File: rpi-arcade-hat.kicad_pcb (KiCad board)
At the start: 2 copper layers, 41.9 x 73.7 mm, 12 parts, among them J1 RASPBERRYPI-40-PIN-GPIO_ARCADE, J2 P2_Joystick, J3 P2_Buttons_ABXY, J4 P2_Buttons_SLSTLR, J5 P1_Joystick, J6 P1_Buttons_ABXY, J7 P1_Buttons_SLSTLR, J8 Hotkey_GNDs

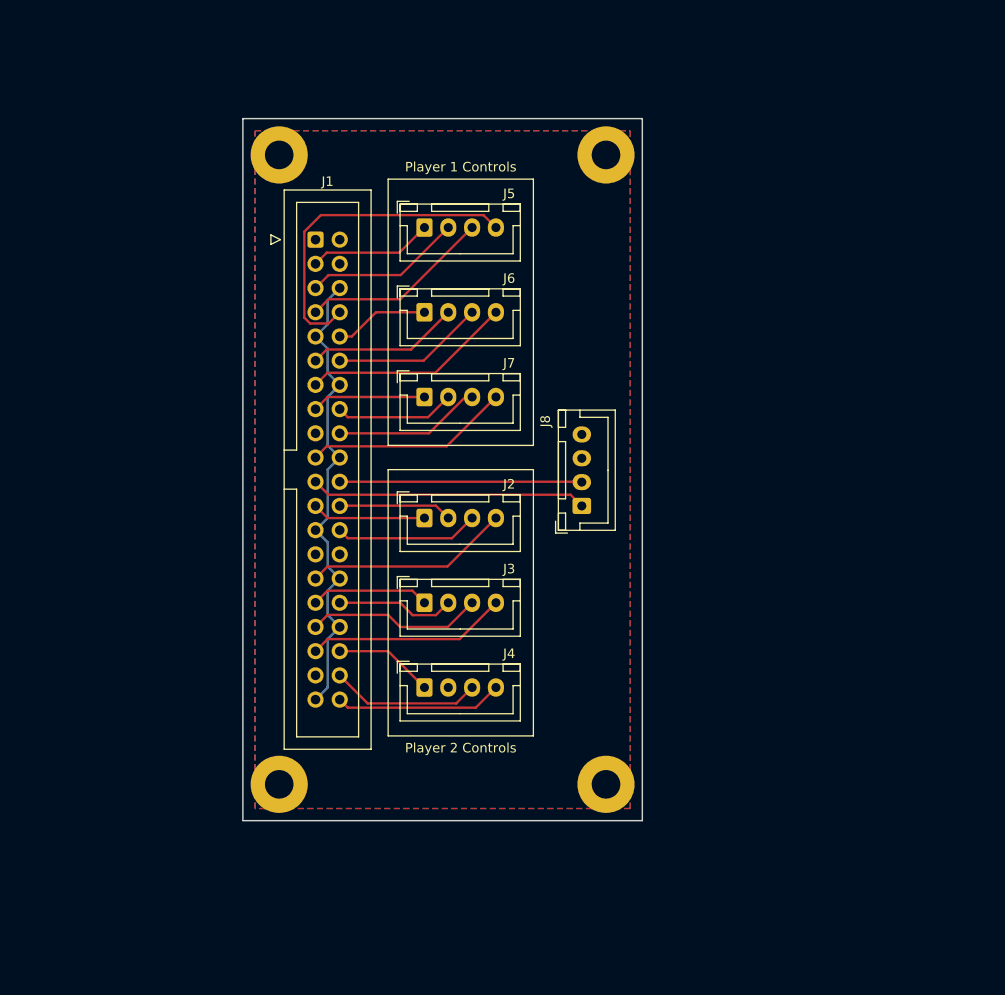
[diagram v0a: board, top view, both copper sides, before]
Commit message: Added 100mm PCBWay layout
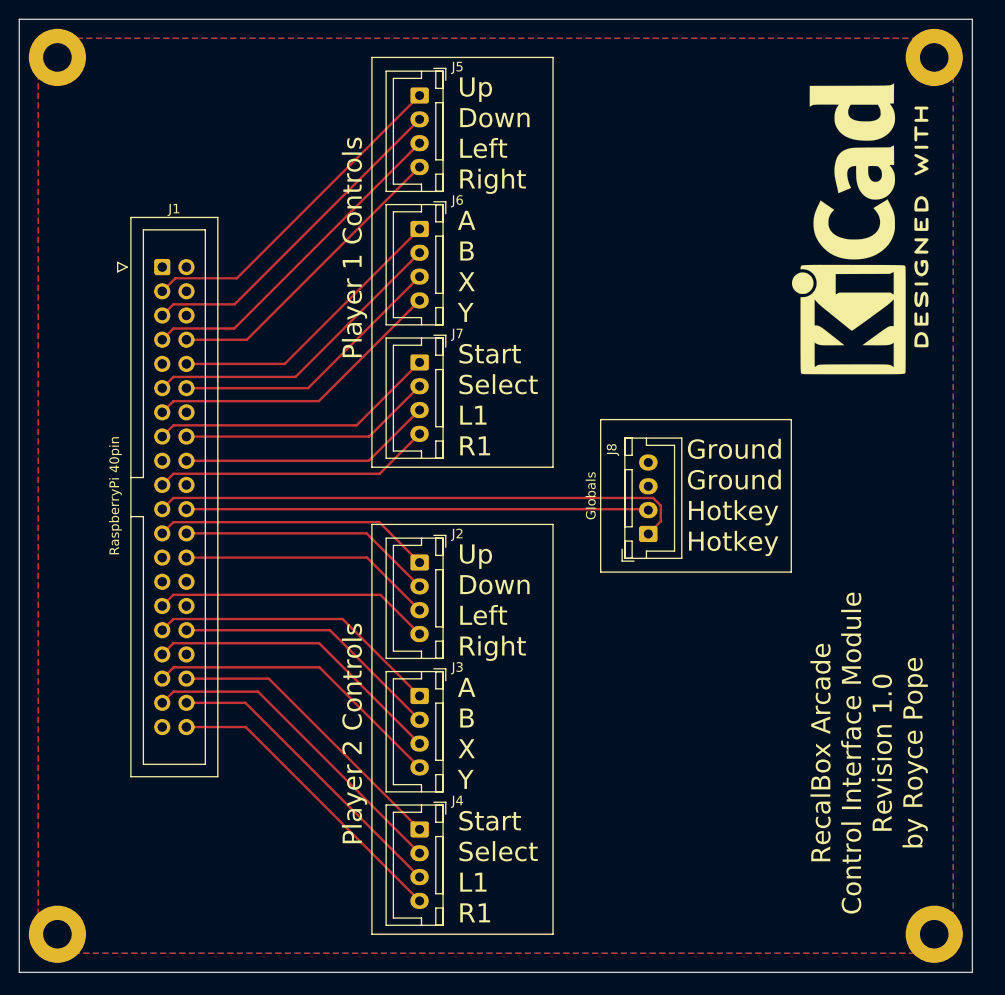
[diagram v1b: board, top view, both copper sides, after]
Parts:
- added REF**: KiCad-Logo2_12mm_SilkScreen, Symbol:KiCad-Logo2_12mm_SilkScreen, F.Cu at (188.0, 70.0)
- moved REF** 37.9 mm to (197.0, 144.0)
- moved REF** 35.9 mm to (197.0, 52.0)
- moved REF** 28.1 mm to (105.0, 144.0)
- moved REF** 25.4 mm to (105.0, 52.0)
- moved J1 16.3 mm to (116.0, 74.0)
- moved J4 14.9 mm to (143.0, 133.0), turned to 270 degrees
- moved J5 13.9 mm to (143.0, 56.0), turned to 270 degrees
- moved J3 9.79 mm to (143.0, 119.0), turned to 270 degrees
- moved J6 8.75 mm to (143.0, 70.0), turned to 270 degrees
- moved J8 7.57 mm to (167.0, 102.0)
- moved J2 4.70 mm to (143.0, 105.0), turned to 270 degrees
- moved J7 3.67 mm to (143.0, 84.0), turned to 270 degrees
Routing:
- net GND: track 50.5 -> 0.00 mm
- net Net-(J1-Pad37): track 0.00 -> 34.5 mm
- net Net-(J1-Pad21): track 29.0 -> 56.6 mm
- net Net-(J1-Pad22): track 25.4 -> 48.5 mm
- net Net-(J1-Pad3): track 13.0 -> 35.5 mm
- net Net-(J1-Pad36): track 10.5 -> 31.0 mm
- net Net-(J1-Pad10): track 9.94 -> 30.3 mm
- net Net-(J1-Pad5): track 16.6 -> 35.5 mm
- net Net-(J1-Pad31): track 12.5 -> 30.8 mm
- net Net-(J1-Pad15): track 12.0 -> 30.2 mm
- net Net-(J1-Pad23): track 12.0 -> 29.2 mm
- net Net-(J1-Pad11): track 16.0 -> 32.9 mm
- net Net-(J1-Pad38): track 15.8 -> 32.0 mm
- net Net-(J1-Pad32): track 12.5 -> 28.4 mm
- net Net-(J1-Pad7): track 20.1 -> 35.5 mm
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- added copper zone on F.Cu, net (none)
- removed copper zone on F.Cu, net Net-(J1-Pad10)
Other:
- board size 41.9 x 73.7 mm -> 100 x 100 mm
- board text added: "A B X Y"
- board text added: "Globals"
- board text added: "Ground Ground Hotkey Hotkey"
- board text added: "RaspberryPi 40pin"
- board text added: "RecalBox Arcade Control Interface Module Revision 1.0 by Royce Pope"
- board text added: "Start Select L1 R1"
- board text added: "Up Down Left Right"

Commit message: Add Part numbers, modify silkscreen, remove unused layers.
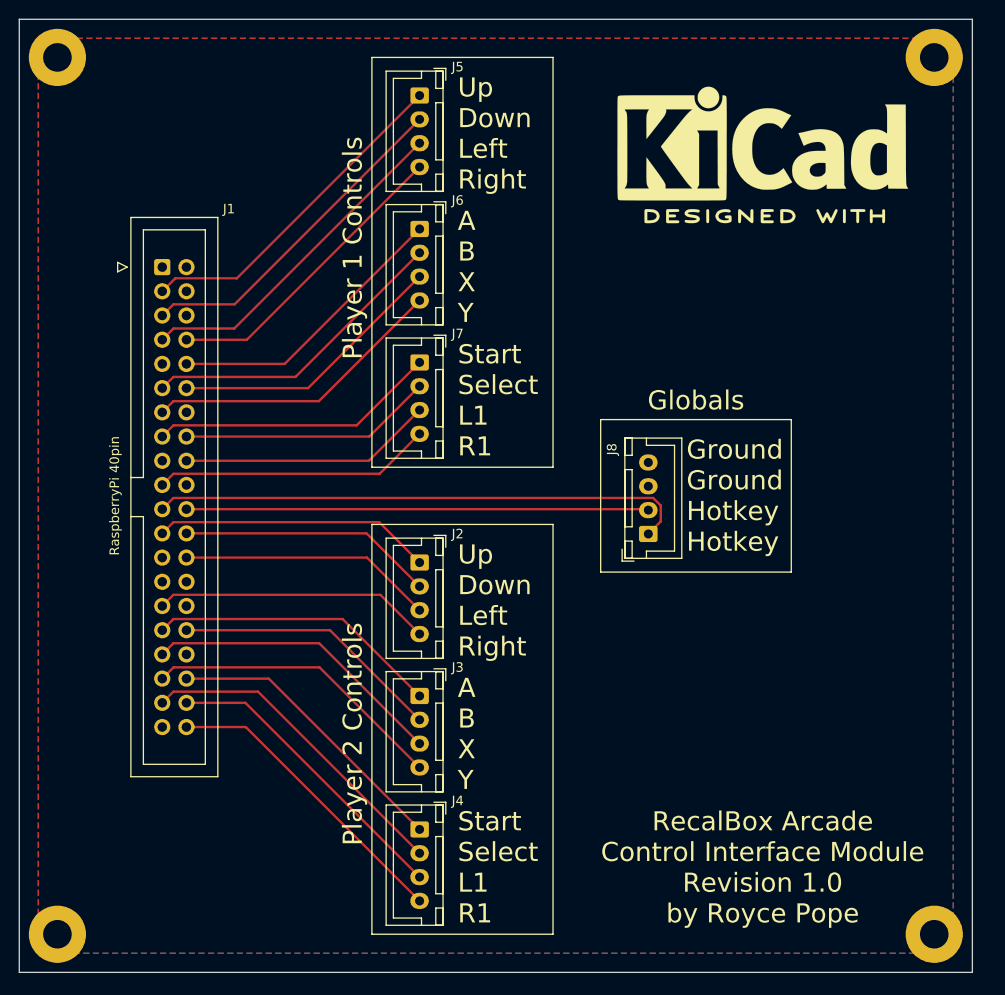
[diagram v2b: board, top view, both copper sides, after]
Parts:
- moved REF** 12.7 mm to (179.0, 61.0), turned to 0 degrees
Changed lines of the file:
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@@
     (0 F.Cu signal)
     (31 B.Cu power)
-    (33 F.Adhes user)
-    (35 F.Paste user)
     (37 F.SilkS user)
     (38 B.Mask user)
     (39 F.Mask user)
-    (40 Dwgs.User user)
     (41 Cmts.User user)
-    (42 Eco1.User user)
-    (43 Eco2.User user)
     (44 Edge.Cuts user)
     (45 Margin user)
-    (46 B.CrtYd user)
+    (46 B.CrtYd user hide)
     (47 F.CrtYd user)
     (49 F.Fab user hide)
@@
   )
   (module Symbol:KiCad-Logo2_12mm_SilkScreen (layer F.Cu)
-    (at 188 70 90)
+    (at 179 61)
     (descr "KiCad Logo")
     (tags "Logo KiCad")
     (attr virtual)
-    (fp_text reference REF** (at 0 -8.89 90) (layer F.SilkS) hide
-      (effects (font (size 1 1) (thickness 0.15)))
-    )
-    (fp_text value KiCad-Logo2_12mm_SilkScreen (at 1.27 10.16 90) (layer F.Fab) hide
+    (fp_text reference REF** (at 0 -8.89) (layer F.SilkS) hide
+      (effects (font (size 1 1) (thickness 0.15)))
+    )
+    (fp_text value KiCad-Logo2_12mm_SilkScreen (at 1.27 10.16) (layer F.Fab) hide
       (effects (font (size 1 1) (thickness 0.15)))
     )
@@
     (descr "Through hole IDC box header, 2x20, 2.54mm pitch, DIN 41651 / IEC 60603-13, double rows, https://docs.google.com/spreadsheets/d/16SsEcesNF15N3Lb4niX7dcUr-NY5_MFPQhobNuNppn4/edit#gid=0")
     (tags "Through hole vertical IDC box header THT 2x20 2.54mm double row")
-    (fp_text reference J1 (at 1.27 -6.1) (layer F.SilkS)
+    (fp_text reference J1 (at 7 -6.1) (layer F.SilkS)
       (effects (font (size 1 1) (thickness 0.15)))
     )
@@
     (effects (font (size 2 2) (thickness 0.15)) (justify left))
   )
-  (gr_text Globals (at 161 98 90) (layer F.SilkS)
-    (effects (font (size 1 1) (thickness 0.15)))
+  (gr_text Globals (at 172 88) (layer F.SilkS)
+    (effects (font (size 2 2) (thickness 0.15)))
   )
   (gr_line (start 162 106) (end 162 90) (layer F.SilkS) (width 0.12))
@@
   (gr_line (start 182 90) (end 182 106) (layer F.SilkS) (width 0.12))
   (gr_line (start 162 90) (end 182 90) (layer F.SilkS) (width 0.12))
-  (gr_text "RecalBox Arcade \nControl Interface Module\nRevision 1.0\nby Royce Pope" (at 190 125 90) (layer F.SilkS)
+  (gr_text "RecalBox Arcade \nControl Interface Module\nRevision 1.0\nby Royce Pope" (at 179 137) (layer F.SilkS)
     (effects (font (size 2 2) (thickness 0.2)))
   )

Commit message: Update to KiCad 6.0
There are new file extensions for KiCad 6.0. I left the old files for backwards compatibility.
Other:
- net class Default removed
